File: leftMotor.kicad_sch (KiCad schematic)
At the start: 0 parts

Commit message: updated motor driver files
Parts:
- added U2: ~, symbol sumo-robot-symbols:TB6612FNG
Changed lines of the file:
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@@
 	(generator_version "9.0")
 	(paper "A4")
+	(symbol
+		(lib_id "sumo-robot-symbols:TB6612FNG")
+		(at 127 107.95 0)
+		(unit 1)
+		(exclude_from_sim no)
+		(in_bom yes)
+		(on_board yes)
+		(dnp no)
+		(property "Reference" "U2"
+			(at 128.016 73.66 0)
+			(effects
+				(font
+					(size 1.27 1.27)
+				)
+			)
+		)
+		(property "Value" "~"
+			(at 144.145 71.12 0)
+			(effects
+				(font
+					(size 1.27 1.27)
+				)
+			)
+		)
+		(property "Footprint" ""
+			(at 127 107.95 0)
+			(effects
+				(font
+					(size 1.27 1.27)
+				)
+				(hide yes)
+			)
+		)
+		(property "Datasheet" ""
+			(at 127 107.95 0)
+			(effects
+				(font
+					(size 1.27 1.27)
+				)
+				(hide yes)
+			)
+		)
+		(property "Description" ""
+			(at 127 107.95 0)
+			(effects
+				(font
+					(size 1.27 1.27)
+				)
+				(hide yes)
+			)
+		)
+		(pin "9"
+		)
+		(pin "18"
+		)
+		(pin "15"
+		)
+		(pin "8"
+		)
+		(pin "12"
+		)
+		(pin "23"
+		)
+		(pin "4"
+		)
+		(pin "19"
+		)
+		(pin "14"
+		)
+		(pin "13"
+		)
+		(pin "21"
+		)
+		(pin "10"
+		)
+		(pin "17"
+		)
+		(pin "3"
+		)
+		(pin "11"
+		)
+		(pin "7"
+		)
+		(pin "22"
+		)
+		(pin "2"
+		)
+		(pin "24"
+		)
+		(pin "6"
+		)
+		(pin "1"
+		)
+		(pin "5"
+		)
+		(pin "20"
+		)
+		(pin "16"
+		)
+		(instances
+			(project ""
+				(path "/f283bc71-7763-4093-b75c-cbe2f5868c12/b92a7e92-a2a7-4561-bf8a-326ace0b674a"
+					(reference "U2")
+					(unit 1)
+				)
+			)
+		)
+	)
 )

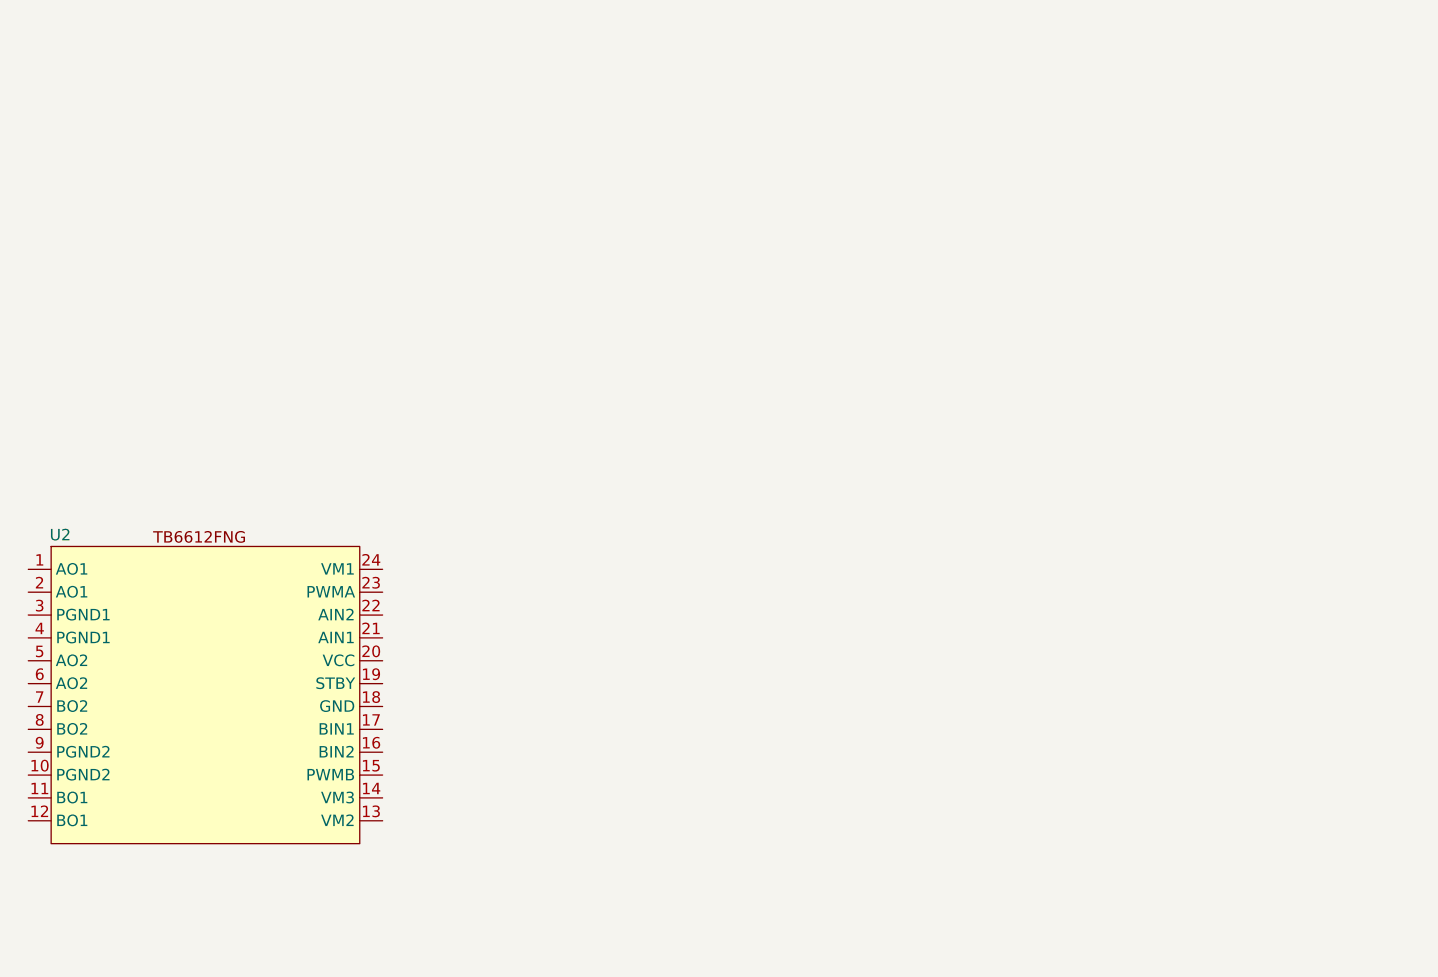
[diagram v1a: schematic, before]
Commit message: added motor functionality to the MCU
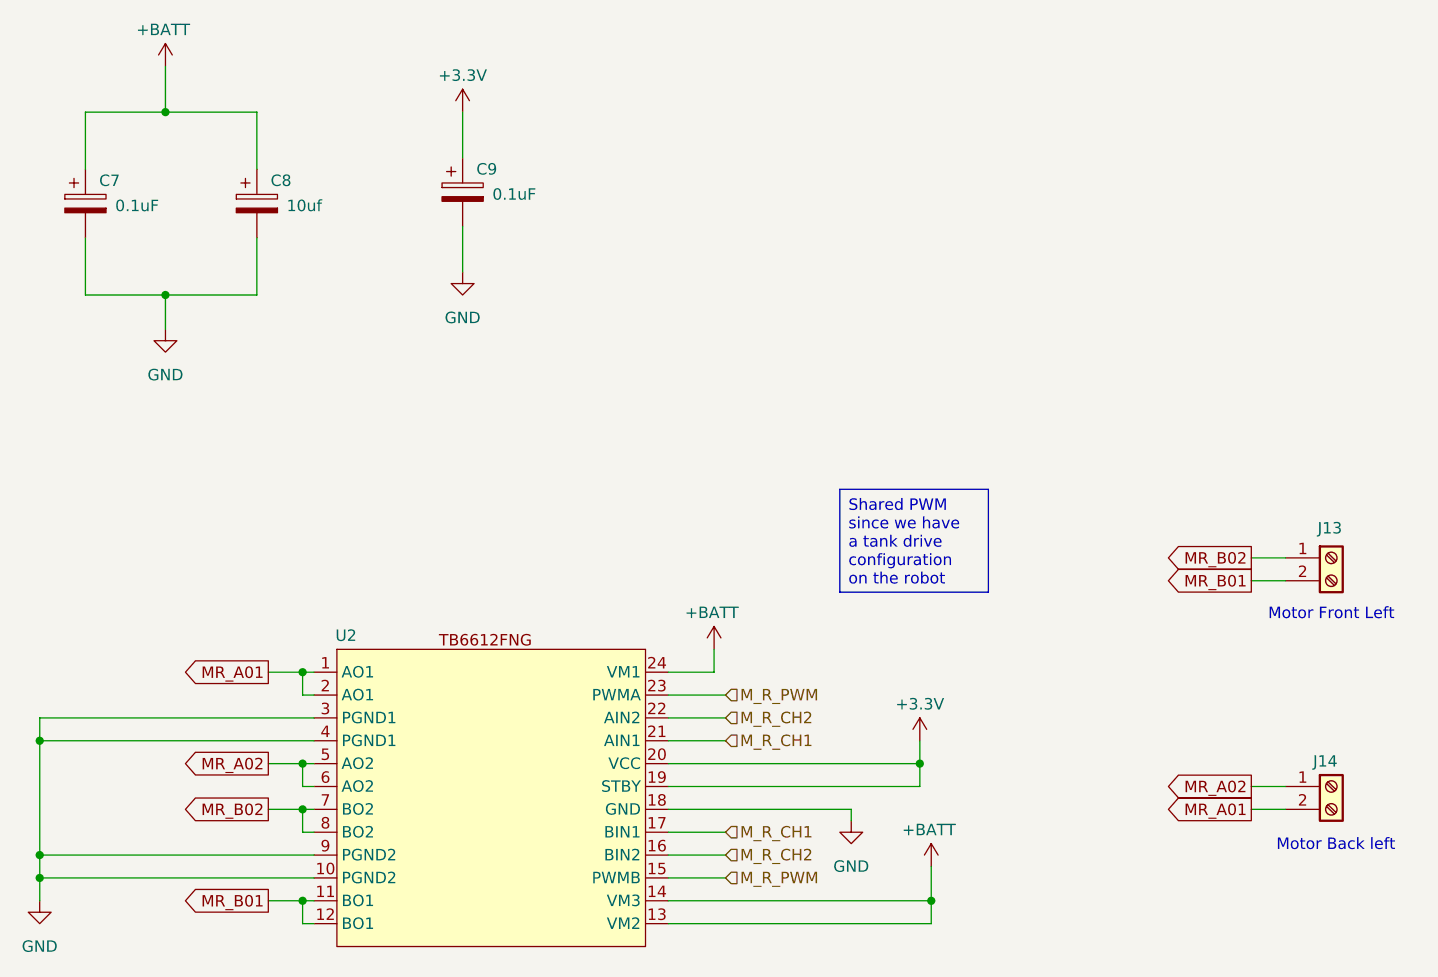
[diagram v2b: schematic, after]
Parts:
- added C7, C9: 0.1uF, symbol Device:C_Polarized
- added C8: 10uf, symbol Device:C_Polarized
- added J13: ~, symbol Connector:Screw_Terminal_01x02
- added J14: Screw_Terminal_01x02, symbol Connector:Screw_Terminal_01x02
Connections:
- net MR_A01: now reaches U2.1 (AO1)
- net MR_A01: now also U2.2 (AO1), J14.2 (Pin_2)
- net GND: now reaches U2.10 (PGND2)
- net GND: now also U2.18 (GND), U2.3 (PGND1), U2.4 (PGND1), U2.9 (PGND2), C7.2, C8.2, C9.2
- net MR_B01: now reaches U2.11 (BO1)
- net MR_B01: now also U2.12 (BO1), J13.2 (Pin_2)
- net +BATT: now reaches U2.13 (VM2)
- net +BATT: now also U2.14 (VM3), U2.24 (VM1), C7.1, C8.1
- net M_R_PWM: now reaches U2.15 (PWMB)
- net M_R_PWM: now also U2.23 (PWMA)
- net M_R_CH2: now reaches U2.16 (BIN2)
- net M_R_CH2: now also U2.22 (AIN2)
- net M_R_CH1: now reaches U2.17 (BIN1)
- net M_R_CH1: now also U2.21 (AIN1)
- net +3.3V: now reaches U2.19 (STBY)
- net +3.3V: now also U2.20 (VCC), C9.1
- net MR_A02: now reaches U2.5 (AO2)
- net MR_A02: now also U2.6 (AO2), J14.1 (Pin_1)
- net MR_B02: now reaches U2.7 (BO2)
- net MR_B02: now also U2.8 (BO2), J13.1 (Pin_1)
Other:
- note added: "Motor Back left"
- note added: "Motor Front Left"

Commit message: added all footprints and step files to components
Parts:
- C7, C8, C9: footprint (none) -> Capacitor_SMD:C_1210_3225Metric
- J13, J14: footprint (none) -> TerminalBlock_Phoenix:TerminalBlock_Phoenix_MKDS-1,5-2_1x02_P5.00mm_Horizontal
- U2: footprint (none) -> Package_SO:SSOP-24_5.3x8.2mm_P0.65mm
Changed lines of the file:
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@@
 			)
 		)
-		(property "Footprint" ""
+		(property "Footprint" "Capacitor_SMD:C_1210_3225Metric"
 			(at 173.6852 39.37 0)
 			(effects
@@
 			)
 		)
-		(property "Footprint" ""
+		(property "Footprint" "TerminalBlock_Phoenix:TerminalBlock_Phoenix_MKDS-1,5-2_1x02_P5.00mm_Horizontal"
 			(at 269.24 76.2 0)
 			(effects
@@
 			)
 		)
-		(property "Footprint" ""
+		(property "Footprint" "Capacitor_SMD:C_1210_3225Metric"
 			(at 131.7752 40.64 0)
 			(effects
@@
 			)
 		)
-		(property "Footprint" ""
+		(property "Footprint" "TerminalBlock_Phoenix:TerminalBlock_Phoenix_MKDS-1,5-2_1x02_P5.00mm_Horizontal"
 			(at 269.24 101.6 0)
 			(effects
@@
 			)
 		)
-		(property "Footprint" ""
+		(property "Footprint" "Package_SO:SSOP-24_5.3x8.2mm_P0.65mm"
 			(at 158.75 119.38 0)
 			(effects
@@
 			)
 		)
-		(property "Footprint" ""
+		(property "Footprint" "Capacitor_SMD:C_1210_3225Metric"
 			(at 150.8252 40.64 0)
 			(effects

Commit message: updated infomration on schematic; started working on layout
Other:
- company: (none) -> Erick Zamora 
- title: (none) -> Miniature Sumo Robot 
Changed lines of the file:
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@@
 	(generator_version "9.0")
 	(paper "A4")
+	(title_block
+		(title "Miniature Sumo Robot ")
+		(date "2025-09-26")
+		(rev "A")
+		(company "Erick Zamora ")
+	)
 	(text "Motor Front Left "
 		(exclude_from_sim no)

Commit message: Updated PCB Layers and Schematics
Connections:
- net GND: no longer U2.10 (PGND2), U2.4 (PGND1)
- net MR_A01: no longer U2.2 (AO1)
- net MR_A02: no longer U2.6 (AO2)
- net MR_B01: no longer U2.12 (BO1)
- net MR_B02: no longer U2.8 (BO2)
- no-connect marks 0 -> 6
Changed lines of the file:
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@@
-	)
-	(junction
-		(at 154.94 88.9)
-		(diameter 0)
-		(color 0 0 0 0)
 	)
 	(junction
@@
 	)
 	(junction
-		(at 154.94 99.06)
-		(diameter 0)
-		(color 0 0 0 0)
-	)
-	(junction
-		(at 125.73 96.52)
-		(diameter 0)
-		(color 0 0 0 0)
-	)
-	(junction
 		(at 139.7 26.67)
 		(diameter 0)
@@
 	)
 	(junction
-		(at 125.73 111.76)
-		(diameter 0)
-		(color 0 0 0 0)
-	)
-	(junction
 		(at 139.7 46.99)
-		(diameter 0)
-		(color 0 0 0 0)
-	)
-	(junction
-		(at 154.94 104.14)
 		(diameter 0)
 		(color 0 0 0 0)
@@
 		(color 0 0 0 0)
 	)
-	(junction
-		(at 154.94 114.3)
-		(diameter 0)
-		(color 0 0 0 0)
-	)
-	(wire
-		(pts
-			(xy 125.73 93.98) (xy 125.73 96.52)
-		)
-		(stroke
-			(width 0)
-			(type default)
-		)
+	(no_connect
+		(at 156.21 116.84)
+	)
+	(no_connect
+		(at 156.21 111.76)
+	)
+	(no_connect
+		(at 156.21 96.52)
+	)
+	(no_connect
+		(at 156.21 106.68)
+	)
+	(no_connect
+		(at 156.21 101.6)
+	)
+	(no_connect
+		(at 156.21 91.44)
 	)
 	(wire
@@
 	(wire
 		(pts
-			(xy 154.94 106.68) (xy 154.94 104.14)
-		)
-		(stroke
-			(width 0)
-			(type default)
-		)
-	)
-	(wire
-		(pts
 			(xy 200.66 88.9) (xy 200.66 86.36)
 		)
@@
 	(wire
 		(pts
-			(xy 125.73 109.22) (xy 125.73 96.52)
+			(xy 125.73 93.98) (xy 125.73 109.22)
 		)
 		(stroke
@@
 	(wire
 		(pts
-			(xy 151.13 104.14) (xy 154.94 104.14)
-		)
-		(stroke
-			(width 0)
-			(type default)
-		)
-	)
-	(wire
-		(pts
 			(xy 224.79 114.3) (xy 224.79 116.84)
 		)
@@
 	(wire
 		(pts
-			(xy 151.13 88.9) (xy 154.94 88.9)
-		)
-		(stroke
-			(width 0)
-			(type default)
-		)
-	)
-	(wire
-		(pts
-			(xy 125.73 111.76) (xy 156.21 111.76)
+			(xy 151.13 88.9) (xy 156.21 88.9)
 		)
 		(stroke
@@
 	(wire
 		(pts
-			(xy 156.21 116.84) (xy 154.94 116.84)
-		)
-		(stroke
-			(width 0)
-			(type default)
-		)
-	)
-	(wire
-		(pts
 			(xy 223.52 99.06) (xy 223.52 96.52)
 		)
@@
 	(wire
 		(pts
-			(xy 154.94 104.14) (xy 156.21 104.14)
+			(xy 151.13 104.14) (xy 156.21 104.14)
 		)
 		(stroke
@@
 	(wire
 		(pts
-			(xy 151.13 114.3) (xy 154.94 114.3)
+			(xy 151.13 114.3) (xy 156.21 114.3)
 		)
 		(stroke
@@
 	(wire
 		(pts
-			(xy 154.94 101.6) (xy 154.94 99.06)
-		)
-		(stroke
-			(width 0)
-			(type default)
-		)
-	)
-	(wire
-		(pts
-			(xy 156.21 106.68) (xy 154.94 106.68)
-		)
-		(stroke
-			(width 0)
-			(type default)
-		)
-	)
-	(wire
-		(pts
-			(xy 154.94 114.3) (xy 156.21 114.3)
-		)
-		(stroke
-			(width 0)
-			(type default)
-		)
-	)
-	(wire
-		(pts
-			(xy 154.94 91.44) (xy 154.94 88.9)
-		)
-		(stroke
-			(width 0)
-			(type default)
-		)
-	)
-	(wire
-		(pts
 			(xy 195.58 93.98) (xy 201.93 93.98)
 		)
@@
 	(wire
 		(pts
-			(xy 156.21 91.44) (xy 154.94 91.44)
-		)
-		(stroke
-			(width 0)
-			(type default)
-		)
-	)
-	(wire
-		(pts
 			(xy 260.35 101.6) (xy 264.16 101.6)
 		)
@@
 	(wire
 		(pts
-			(xy 151.13 99.06) (xy 154.94 99.06)
-		)
-		(stroke
-			(width 0)
-			(type default)
-		)
-	)
-	(wire
-		(pts
 			(xy 195.58 111.76) (xy 201.93 111.76)
 		)
@@
 	(wire
 		(pts
-			(xy 156.21 101.6) (xy 154.94 101.6)
-		)
-		(stroke
-			(width 0)
-			(type default)
-		)
-	)
-	(wire
-		(pts
 			(xy 195.58 114.3) (xy 224.79 114.3)
 		)
@@
 	(wire
 		(pts
-			(xy 125.73 114.3) (xy 125.73 111.76)
-		)
-		(stroke
-			(width 0)
-			(type default)
-		)
-	)
-	(wire
-		(pts
-			(xy 125.73 111.76) (xy 125.73 109.22)
+			(xy 125.73 109.22) (xy 125.73 114.3)
 		)
 		(stroke
@@
 	(wire
 		(pts
-			(xy 154.94 88.9) (xy 156.21 88.9)
-		)
-		(stroke
-			(width 0)
-			(type default)
-		)
-	)
-	(wire
-		(pts
 			(xy 149.86 33.02) (xy 149.86 26.67)
 		)
@@
 	(wire
 		(pts
-			(xy 125.73 96.52) (xy 156.21 96.52)
-		)
-		(stroke
-			(width 0)
-			(type default)
-		)
-	)
-	(wire
-		(pts
 			(xy 149.86 40.64) (xy 149.86 46.99)
 		)
@@
 	(wire
 		(pts
-			(xy 154.94 116.84) (xy 154.94 114.3)
-		)
-		(stroke
-			(width 0)
-			(type default)
-		)
-	)
-	(wire
-		(pts
 			(xy 149.86 26.67) (xy 139.7 26.67)
 		)
@@
 	(wire
 		(pts
-			(xy 154.94 99.06) (xy 156.21 99.06)
-		)
-		(stroke
+			(xy 151.13 99.06) (xy 156.21 99.06)
+		)
+		(stroke
